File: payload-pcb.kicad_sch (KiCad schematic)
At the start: 4 parts

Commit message: more cleanup and added notes for review
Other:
- note added: "README LIBRARIES MODELS"
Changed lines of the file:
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@@
 		(company "WVU Unviersity Rover Challenge")
+	)
+	(text "README\nLIBRARIES\nMODELS"
+		(exclude_from_sim no)
+		(at 202.184 28.702 0)
+		(effects
+			(font
+				(size 2.54 2.54)
+				(thickness 0.508)
+				(bold yes)
+				(color 255 0 0 1)
+			)
+			(justify left top)
+		)
 	)
 	(text "Payload PCB"
@@
 	(text "West Virginia University: University Rover Challenge (URC)\nby Austin Driggs (2025-2026)"
 		(exclude_from_sim no)
-		(at 148.844 38.862 0)
+		(at 148.844 39.37 0)
 		(effects
 			(font
@@
 		(stroke
 			(width 0)
-			(type default)
+			(type dash)
 		)
 	)
@@
 			)
 		)
-		(property "MANUFACTURER" ""
-			(at 67.31 171.45 0)
-			(effects
-				(font
-					(size 1.27 1.27)
-				)
-				(hide yes)
-			)
-		)
-		(property "PARTREV" ""
-			(at 67.31 171.45 0)
-			(effects
-				(font
-					(size 1.27 1.27)
-				)
-				(hide yes)
-			)
-		)
-		(property "STANDARD" ""
+		(property "Manufacturer" ""
+			(at 67.31 171.45 0)
+			(effects
+				(font
+					(size 1.27 1.27)
+				)
+				(hide yes)
+			)
+		)
+		(property "Manufacturer Part Number" ""
+			(at 67.31 171.45 0)
+			(effects
+				(font
+					(size 1.27 1.27)
+				)
+				(hide yes)
+			)
+		)
+		(property "Vendor" ""
+			(at 67.31 171.45 0)
+			(effects
+				(font
+					(size 1.27 1.27)
+				)
+				(hide yes)
+			)
+		)
+		(property "Vendor Part Number" ""
+			(at 67.31 171.45 0)
+			(effects
+				(font
+					(size 1.27 1.27)
+				)
+				(hide yes)
+			)
+		)
+		(property "Comments" ""
+			(at 67.31 171.45 0)
+			(effects
+				(font
+					(size 1.27 1.27)
+				)
+				(hide yes)
+			)
+		)
+		(property "Notes" ""
 			(at 67.31 171.45 0)
 			(effects
@@
 			)
 		)
-		(property "MANUFACTURER" ""
-			(at 120.65 171.45 0)
-			(effects
-				(font
-					(size 1.27 1.27)
-				)
-				(hide yes)
-			)
-		)
-		(property "PARTREV" ""
-			(at 120.65 171.45 0)
-			(effects
-				(font
-					(size 1.27 1.27)
-				)
-				(hide yes)
-			)
-		)
-		(property "STANDARD" ""
+		(property "Manufacturer" ""
+			(at 120.65 171.45 0)
+			(effects
+				(font
+					(size 1.27 1.27)
+				)
+				(hide yes)
+			)
+		)
+		(property "Manufacturer Part Number" ""
+			(at 120.65 171.45 0)
+			(effects
+				(font
+					(size 1.27 1.27)
+				)
+				(hide yes)
+			)
+		)
+		(property "Vendor" ""
+			(at 120.65 171.45 0)
+			(effects
+				(font
+					(size 1.27 1.27)
+				)
+				(hide yes)
+			)
+		)
+		(property "Vendor Part Number" ""
+			(at 120.65 171.45 0)
+			(effects
+				(font
+					(size 1.27 1.27)
+				)
+				(hide yes)
+			)
+		)
+		(property "Comments" ""
+			(at 120.65 171.45 0)
+			(effects
+				(font
+					(size 1.27 1.27)
+				)
+				(hide yes)
+			)
+		)
+		(property "Notes" ""
 			(at 120.65 171.45 0)
 			(effects
@@
 			)
 		)
-		(property "MANUFACTURER" ""
-			(at 102.87 171.45 0)
-			(effects
-				(font
-					(size 1.27 1.27)
-				)
-				(hide yes)
-			)
-		)
-		(property "PARTREV" ""
-			(at 102.87 171.45 0)
-			(effects
-				(font
-					(size 1.27 1.27)
-				)
-				(hide yes)
-			)
-		)
-		(property "STANDARD" ""
+		(property "Manufacturer" ""
+			(at 102.87 171.45 0)
+			(effects
+				(font
+					(size 1.27 1.27)
+				)
+				(hide yes)
+			)
+		)
+		(property "Manufacturer Part Number" ""
+			(at 102.87 171.45 0)
+			(effects
+				(font
+					(size 1.27 1.27)
+				)
+				(hide yes)
+			)
+		)
+		(property "Vendor" ""
+			(at 102.87 171.45 0)
+			(effects
+				(font
+					(size 1.27 1.27)
+				)
+				(hide yes)
+			)
+		)
+		(property "Vendor Part Number" ""
+			(at 102.87 171.45 0)
+			(effects
+				(font
+					(size 1.27 1.27)
+				)
+				(hide yes)
+			)
+		)
+		(property "Comments" ""
+			(at 102.87 171.45 0)
+			(effects
+				(font
+					(size 1.27 1.27)
+				)
+				(hide yes)
+			)
+		)
+		(property "Notes" ""
 			(at 102.87 171.45 0)
 			(effects
@@
 			)
 		)
-		(property "MANUFACTURER" ""
-			(at 85.09 171.45 0)
-			(effects
-				(font
-					(size 1.27 1.27)
-				)
-				(hide yes)
-			)
-		)
-		(property "PARTREV" ""
-			(at 85.09 171.45 0)
-			(effects
-				(font
-					(size 1.27 1.27)
-				)
-				(hide yes)
-			)
-		)
-		(property "STANDARD" ""
-			(at 85.09 171.45 0)
-			(effects
+		(property "Manufacturer" ""
+			(at 85.09 171.45 0)
+			(effects
+				(font
+					(size 1.27 1.27)
+				)
+				(hide yes)
+			)
+		)
+		(property "Manufacturer Part Number" ""
+			(at 85.09 171.45 0)
+			(effects
+				(font
+					(size 1.27 1.27)
+				)
+				(hide yes)
+			)
+		)
+		(property "Vendor" ""
+			(at 85.09 171.45 0)
+			(effects
+				(font
+					(size 1.27 1.27)
+				)
+				(hide yes)
+			)
+		)
+		(property "Vendor Part Number" ""
+			(at 85.09 171.45 0)
+			(effects
+				(font
+					(size 1.27 1.27)
+				)
+				(hide yes)
+			)
+		)
+		(property "Comments" ""
+			(at 85.09 171.45 0)
+			(effects
+				(font
+					(size 1.27 1.27)
+				)
+				(hide yes)
+			)
+		)
+		(property "Notes" ""
+			(at 85.09 171.45 0)
+			(effects

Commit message: pcb review session notes
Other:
- note added: "README LIBRARIES MODELS DE10 acrylic cover"
- note removed: "README LIBRARIES MODELS"
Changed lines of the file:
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@@
 		(company "WVU Unviersity Rover Challenge")
 	)
-	(text "README\nLIBRARIES\nMODELS"
+	(text "README\nLIBRARIES\nMODELS\n\nDE10 acrylic cover\n"
 		(exclude_from_sim no)
-		(at 202.184 28.702 0)
+		(at 201.93 18.288 0)
 		(effects
 			(font

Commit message: major rework again after the meeting
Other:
- removed sheet LEDs
- added sheet USB (usb.kicad_sch)
- note removed: "README LIBRARIES MODELS DE10 acrylic cover"
- moved on the sheet: H1, H2, H3, H4

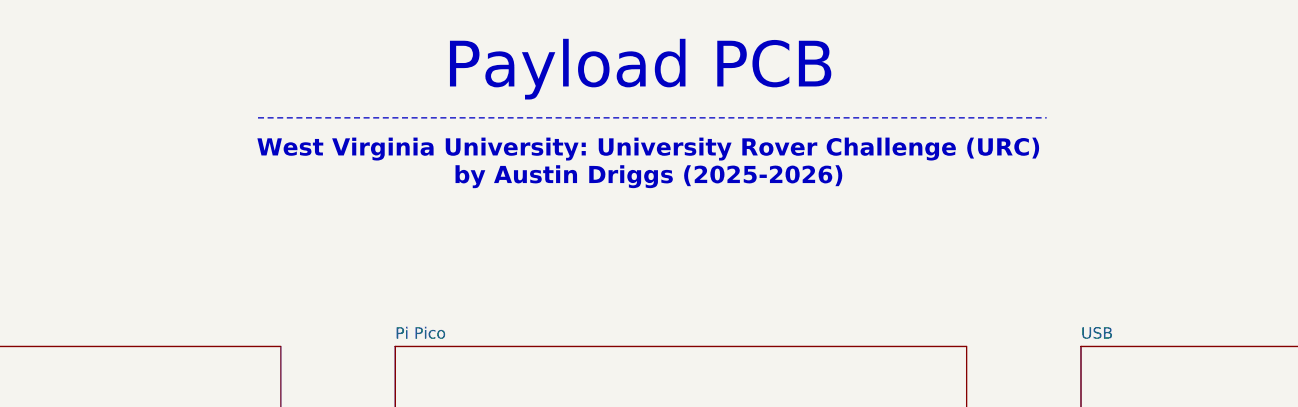
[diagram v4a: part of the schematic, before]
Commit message: major finishing touches:     - major rework for v5.1     - silkscreen and stuff     - impednace for USB and CAN lines     - schematic comments     - symbol, footprint, and model library updates
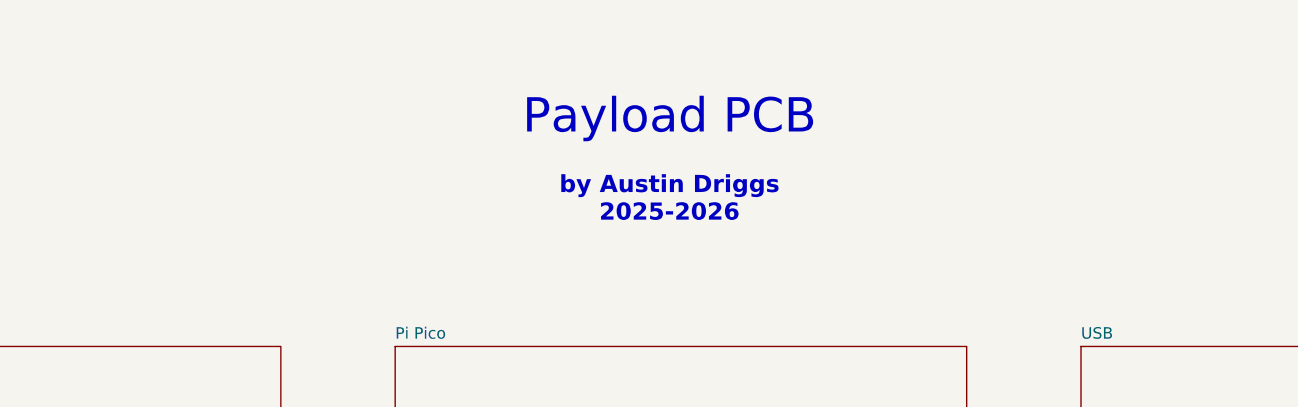
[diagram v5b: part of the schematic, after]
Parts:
- H1, H2, H3, H4: now left out of the parts list
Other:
- note added: "by Austin Driggs 2025-2026"
- note removed: "West Virginia University: University Rover Challenge (URC) by Austin Driggs (2025-2026)"
- company: WVU Unviersity Rover Challenge -> WVU Unviersity Rover Challenge (URC)
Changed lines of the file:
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@@
 	(title_block
 		(title "Payload PCB")
-		(date "2025-12-02")
-		(rev "v5.0")
-		(company "WVU Unviersity Rover Challenge")
+		(date "2025-01-02")
+		(rev "v5.1")
+		(company "WVU Unviersity Rover Challenge (URC)")
 	)
 	(text "Payload PCB"
 		(exclude_from_sim no)
-		(at 145.288 28.702 0)
+		(at 148.59 34.29 0)
 		(effects
 			(font
-				(size 5.08 5.08)
+				(size 3.81 3.81)
 				(thickness 0.635)
 			)
 		)
 	)
-	(text "West Virginia University: University Rover Challenge (URC)\nby Austin Driggs (2025-2026)"
+	(text "by Austin Driggs\n2025-2026"
 		(exclude_from_sim no)
-		(at 146.304 39.37 0)
+		(at 148.59 43.434 0)
 		(effects
 			(font
@@
 				(bold yes)
 			)
-		)
-	)
-	(polyline
-		(pts
-			(xy 102.87 34.29) (xy 190.5 34.29)
-		)
-		(stroke
-			(width 0)
-			(type dash)
 		)
 	)
@@
 		(unit 1)
 		(exclude_from_sim no)
-		(in_bom yes)
-		(on_board yes)
+		(in_bom no)
+		(on_board no)
 		(dnp no)
 		(property "Reference" "H1"
@@
 		)
 		(property "Notes" ""
+			(at 71.12 171.45 0)
+			(effects
+				(font
+					(size 1.27 1.27)
+				)
+				(hide yes)
+			)
+		)
+		(property "KLC_S4.2_3V3OUT" ""
+			(at 71.12 171.45 0)
+			(effects
+				(font
+					(size 1.27 1.27)
+				)
+				(hide yes)
+			)
+		)
+		(property "KLC_S4.2_VCC" ""
 			(at 71.12 171.45 0)
 			(effects
@@
 		(unit 1)
 		(exclude_from_sim no)
-		(in_bom yes)
+		(in_bom no)
 		(on_board yes)
 		(dnp no)
@@
 		)
 		(property "Notes" ""
+			(at 124.46 171.45 0)
+			(effects
+				(font
+					(size 1.27 1.27)
+				)
+				(hide yes)
+			)
+		)
+		(property "KLC_S4.2_3V3OUT" ""
+			(at 124.46 171.45 0)
+			(effects
+				(font
+					(size 1.27 1.27)
+				)
+				(hide yes)
+			)
+		)
+		(property "KLC_S4.2_VCC" ""
 			(at 124.46 171.45 0)
 			(effects
@@
 		(unit 1)
 		(exclude_from_sim no)
-		(in_bom yes)
+		(in_bom no)
 		(on_board yes)
 		(dnp no)
@@
 		)
 		(property "Notes" ""
+			(at 106.68 171.45 0)
+			(effects
+				(font
+					(size 1.27 1.27)
+				)
+				(hide yes)
+			)
+		)
+		(property "KLC_S4.2_3V3OUT" ""
+			(at 106.68 171.45 0)
+			(effects
+				(font
+					(size 1.27 1.27)
+				)
+				(hide yes)
+			)
+		)
+		(property "KLC_S4.2_VCC" ""
 			(at 106.68 171.45 0)
 			(effects
@@
 		(unit 1)
 		(exclude_from_sim no)
-		(in_bom yes)
-		(on_board yes)
+		(in_bom no)
+		(on_board no)
 		(dnp no)
 		(property "Reference" "H2"
@@
 			(at 88.9 171.45 0)
 			(effects
+				(font
+					(size 1.27 1.27)
+				)
+				(hide yes)
+			)
+		)
+		(property "KLC_S4.2_3V3OUT" ""
+			(at 88.9 171.45 0)
+			(effects
+				(font
+					(size 1.27 1.27)
+				)
+				(hide yes)
+			)
+		)
+		(property "KLC_S4.2_VCC" ""
+			(at 88.9 171.45 0)
+			(effects
